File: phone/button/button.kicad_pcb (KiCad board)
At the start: 2 copper layers, 25 x 17 mm, 2 parts, among them J1 Conn_01x02, SW1 SW_Push

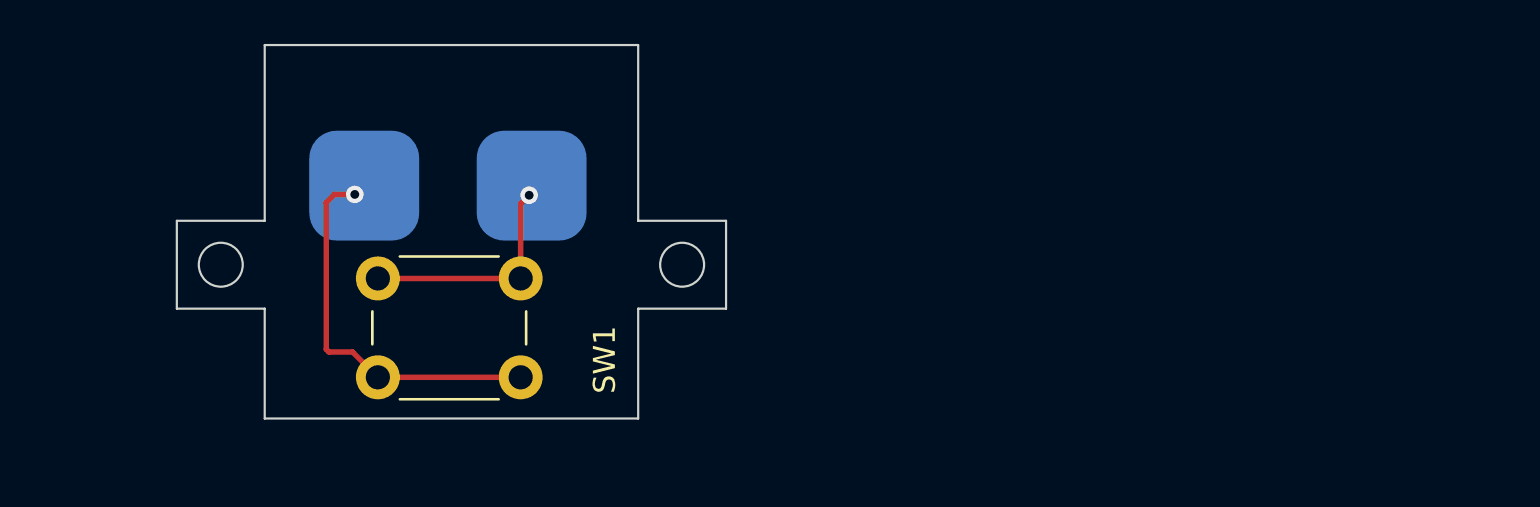
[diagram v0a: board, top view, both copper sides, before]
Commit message: edited switch pcb and made buttons, add speaker grill , add switch pcb support
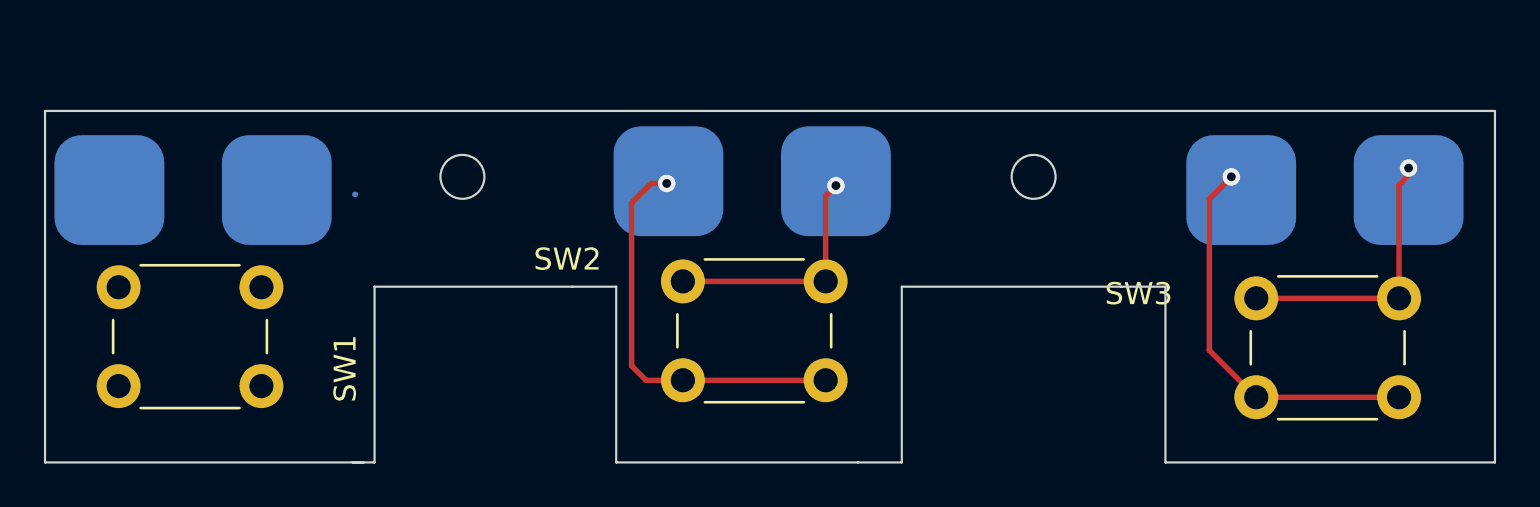
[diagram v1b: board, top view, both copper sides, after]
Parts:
- added J2: Conn_01x02, solderwirepad_1_02_SMD:SolderWirePad_1x02_SMD_5x5mm, B.Cu at (152.0, 97.2)
- added J3: Conn_01x02, solderwirepad_1_02_SMD:SolderWirePad_1x02_SMD_5x5mm, B.Cu at (178.1, 97.6)
- added SW2: SW_Push, Button_Switch_THT:SW_PUSH_6mm, F.Cu at (145.0, 101.8)
- added SW3: SW_Push, Button_Switch_THT:SW_PUSH_6mm, F.Cu at (171.1, 102.5)
- moved SW1 11.8 mm to (119.3, 102.0)
- moved J1 11.6 mm to (126.5, 97.6)
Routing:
- net Net-(SW2-Pad2): track 0.00 -> 18.5 mm, vias 0 -> 1
- net Net-(J1-Pad1): track 18.1 -> 0.03 mm, vias 1 -> 0
- net Net-(SW3-Pad2): track 0.00 -> 17.8 mm, vias 0 -> 1
- net Net-(SW3-Pad1): track 0.00 -> 12.6 mm, vias 0 -> 1
- net Net-(SW2-Pad1): track 0.00 -> 11.1 mm, vias 0 -> 1
- net Net-(J1-Pad2): track 11.0 -> 0.00 mm, vias 1 -> 0
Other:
- board size 25 x 17 mm -> 66 x 16 mm
